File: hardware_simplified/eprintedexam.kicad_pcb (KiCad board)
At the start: 2 copper layers, 103 x 98.5 mm, 41 parts, among them J1 Conn_01x04, J2 Conn_01x08, Q1 2N7002, Q2 2N7002, Q3 2N7002, Q4 2N7002, Q5 2N7002, Q6 2N7002, SW1 SW_Push, SW2 SW_Push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

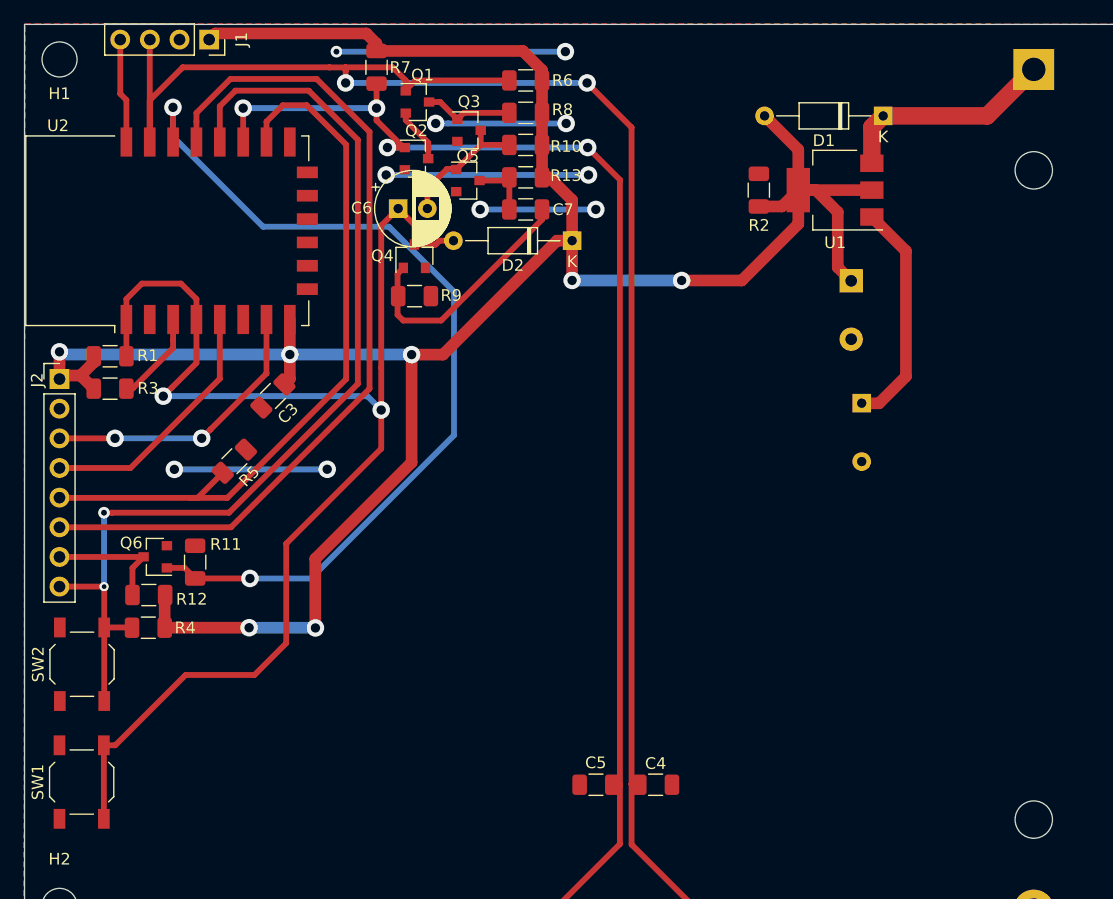
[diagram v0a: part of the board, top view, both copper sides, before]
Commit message: fixed monostable and improved pcb layout
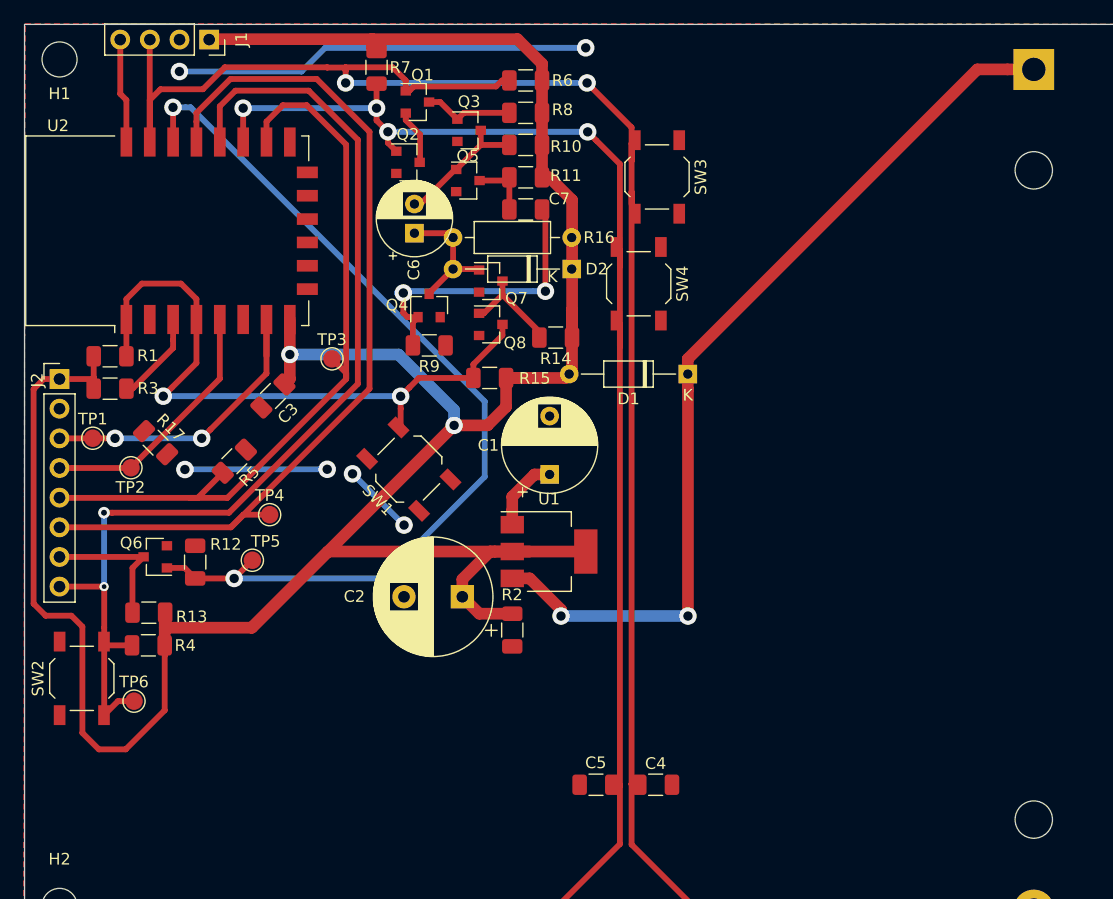
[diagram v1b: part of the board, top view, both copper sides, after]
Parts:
- removed the R11 at (105.9, 92.2)
- added Q7: 2N7002, Package_TO_SOT_SMD:SOT-23, F.Cu at (131.2, 68.1)
- added Q8: 2N7002, Package_TO_SOT_SMD:SOT-23, F.Cu at (131.2, 71.8)
- added R12: 10k, Resistor_SMD:R_1206_3216Metric, F.Cu at (105.9, 92.2)
- added R14: 22k, Resistor_SMD:R_1206_3216Metric, F.Cu at (136.8, 73.0)
- added R15: 22k, Resistor_SMD:R_1206_3216Metric, F.Cu at (131.1, 76.4)
- added R16: 10k, Resistor_THT:R_Axial_DIN0207_L6.3mm_D2.5mm_P10.16mm_Horizontal, F.Cu at (138.1, 64.4)
- added R17: 0, Resistor_SMD:R_1206_3216Metric, F.Cu at (102.5, 82.0)
- added SW3: SW_Push, Button_Switch_SMD:SW_SPST_TL3342, F.Cu at (145.4, 59.2)
- added SW4: SW_Push, Button_Switch_SMD:SW_SPST_TL3342, F.Cu at (143.9, 68.3)
- added TP1: TestPoint, TestPoint:TestPoint_Pad_D1.5mm, F.Cu at (97.1, 81.6)
- added TP2: TestPoint, TestPoint:TestPoint_Pad_D1.5mm, F.Cu at (100.4, 84.1)
- added TP3: TestPoint, TestPoint:TestPoint_Pad_D1.5mm, F.Cu at (117.6, 74.8)
- added TP4: TestPoint, TestPoint:TestPoint_Pad_D1.5mm, F.Cu at (112.3, 88.1)
- added TP5: TestPoint, TestPoint:TestPoint_Pad_D1.5mm, F.Cu at (110.8, 92.0)
- added TP6: TestPoint, TestPoint:TestPoint_Pad_D1.5mm, F.Cu at (100.7, 104.1)
- C1, C2: moved to F.Cu
- moved R2 43.2 mm to (133.1, 98.0), turned to 270 degrees
- moved C2 42.9 mm to (128.8, 95.2), turned to 180 degrees
- moved U1 39.5 mm to (136.2, 91.3), turned to 0 degrees
- moved SW1 38.8 mm to (124.2, 84.2), turned to 135 degrees
- moved D1 27.7 mm to (148.1, 76.1)
- moved C1 27.4 mm to (136.2, 84.7), turned to 90 degrees
- moved Q4 4.40 mm to (125.9, 70.2)
- moved R9 4.40 mm to (125.9, 73.6)
- moved C6 2.53 mm to (124.7, 64.0), turned to 90 degrees
- moved D2 2.43 mm to (138.1, 67.1)
- moved R13 1.51 mm to (101.9, 96.5)
- moved R4 1.51 mm to (101.9, 99.3)
- moved SW2 1.21 mm to (96.2, 102.1)
- moved Q2 0.80 mm to (124.1, 57.9)
- renumbered R13 to R11, R12 to R13
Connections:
- C6 pad 1: nrst -> Net-(C6-Pad1)
- D2 pad 2: nrst -> Net-(C6-Pad1)
- Q4 pad 3: nrst -> Net-(C6-Pad1)
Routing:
- net Net-(BT1-Pad1): track 19.0 -> 78.7 mm, vias 0 -> 2
- net nrst: track 114.6 -> 57.1 mm
- net VCC: track 206.9 -> 237.2 mm, vias 7 -> 2
- net GND: track 71.1 -> 54.1 mm, vias 10 -> 6
- net Net-(C1-Pad1): track 19.6 -> 6.39 mm
- net Net-(C6-Pad1): track 0.00 -> 11.2 mm
- net Net-(Q7-Pad3): track 0.00 -> 8.81 mm
- net Net-(C7-Pad2): track 21.3 -> 25.7 mm, vias 0 -> 2
- net spi-busy,flash: track 86.8 -> 91.1 mm
- net prv: track 131.2 -> 135.1 mm
- net spi-dc: track 73.9 -> 77.6 mm
- net spi-mosi: track 24.7 -> 27.8 mm
- net nxt: track 165.7 -> 168.6 mm
- net spi-rst: track 77.4 -> 80.0 mm
- net spi-cs: track 63.1 -> 65.3 mm
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
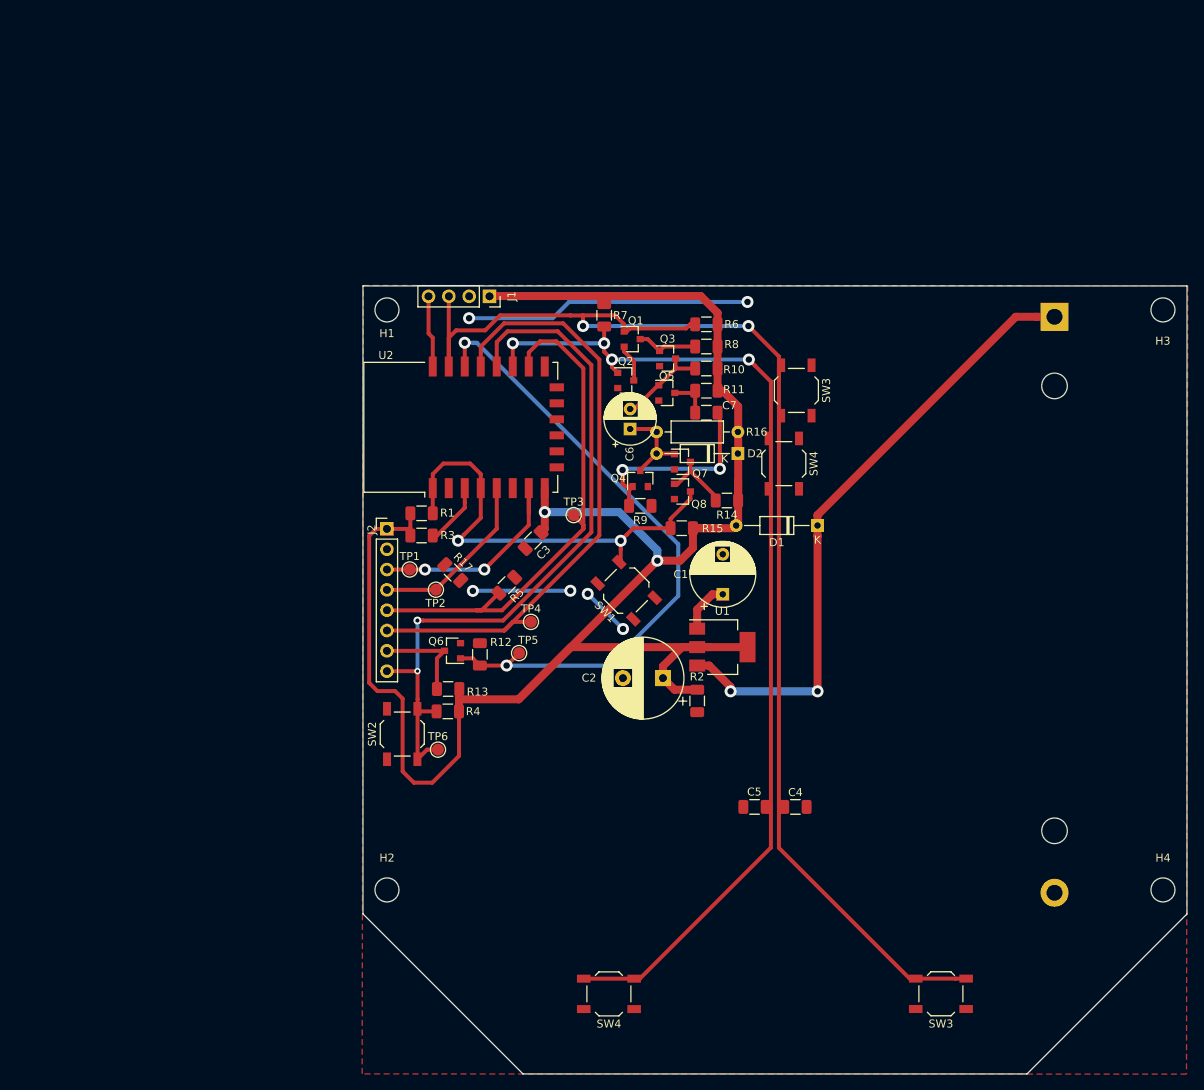
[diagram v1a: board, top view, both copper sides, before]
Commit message: changed nxt and prv port
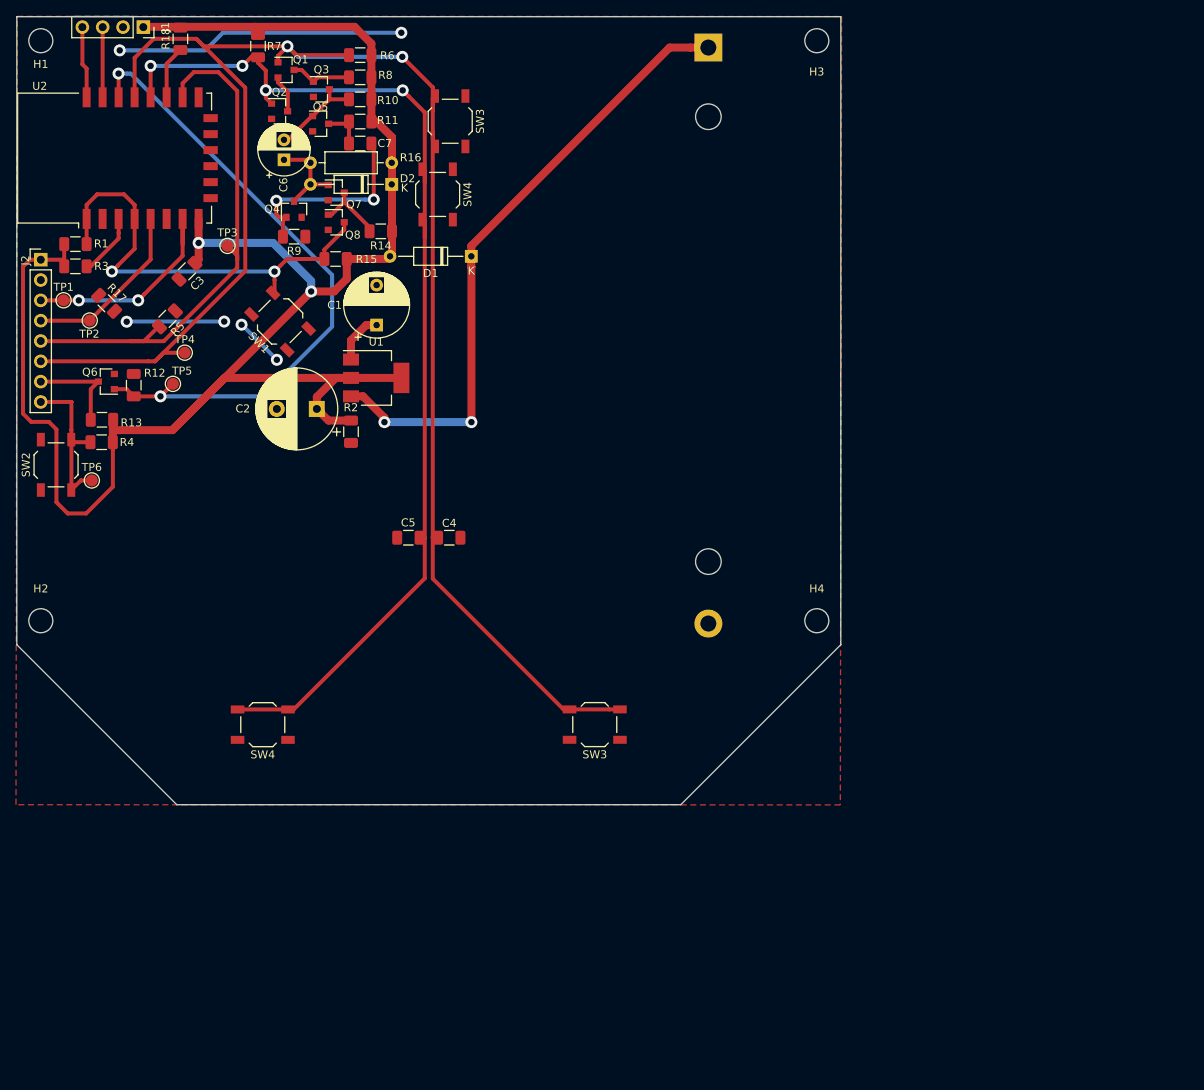
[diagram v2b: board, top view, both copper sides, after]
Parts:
- removed the SW3 at (145.4, 59.2)
- removed the SW3 at (163.5, 134.6)
- removed the SW4 at (143.9, 68.3)
- removed the SW4 at (122.0, 134.6)
- added R18: 10k, Resistor_SMD:R_1206_3216Metric, F.Cu at (68.5, 15.2)
- added SW3: SW_Push, Button_Switch_SMD:SW_SPST_TL3342, F.Cu at (102.2, 25.5)
- added SW3: SW_Push, Button_Switch_SMD:SW_SPST_TL3342, F.Cu at (120.2, 101.0)
- added SW4: SW_Push, Button_Switch_SMD:SW_SPST_TL3342, F.Cu at (100.6, 34.7)
- added SW4: SW_Push, Button_Switch_SMD:SW_SPST_TL3342, F.Cu at (78.8, 101.0)
- R14: value 22k -> 18k
- R15: value 22k -> 1k
- R6, R7: value 10k -> 5k
- moved C2 54.8 mm to (85.5, 61.5)
- moved C4 54.8 mm to (102.1, 77.6)
- moved D1 54.8 mm to (104.8, 42.4)
- moved H4 54.8 mm to (148.0, 88.0)
- moved Q4 54.8 mm to (82.7, 36.5)
- moved R14 54.8 mm to (93.5, 39.3)
- moved R2 54.8 mm to (89.8, 64.3)
- moved SW2 54.8 mm to (52.9, 68.5)
- moved BT1 54.8 mm to (134.4, 16.3)
- moved H1 54.8 mm to (51.0, 15.5)
- moved H2 54.8 mm to (51.0, 88.0)
- moved H3 54.8 mm to (148.0, 15.5)
- moved J1 54.8 mm to (63.8, 13.8)
- moved Q2 54.8 mm to (80.8, 24.3)
- moved Q7 54.8 mm to (87.9, 34.5)
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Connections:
- J1 pad 3: nxt -> Net-(J1-Pad3)
- J2 pad 6: spi-dc -> nxt
- J2 pad 8: spi-busy,flash -> prv
- R4 pad 2: spi-busy,flash -> prv
- R6 pad 1: nxt -> VCC
- R6 pad 2: VCC -> nxt
- SW2 pad 2: spi-busy,flash -> prv
- TP4 pad 1: spi-dc -> nxt
- TP6 pad 1: spi-busy,flash -> prv
- U2 pad 17: prv -> Net-(R18-Pad1)
- U2 pad 18: spi-busy,flash -> prv
- U2 pad 19: spi-dc -> nxt
- U2 pad 21: nxt -> Net-(J1-Pad3)
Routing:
- net spi-busy,flash: track 91.1 -> 0.00 mm, vias 2 -> 0
- net spi-dc: track 77.6 -> 0.00 mm
- net nxt: track 168.6 -> 217.5 mm
- net prv: track 135.1 -> 159.0 mm
- net Net-(J1-Pad3): track 0.00 -> 8.68 mm
- net Net-(R18-Pad1): track 0.00 -> 6.62 mm
- net VCC: track 237.2 -> 240.6 mm
- net spi-cs: track 65.3 -> 67.2 mm
